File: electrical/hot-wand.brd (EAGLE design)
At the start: 112 x 72 mm, 186 parts, among them IC1 12V R-78K12-2.0, IC2 3V3 R-78K3.3, Q1 STP19NF20, Q2 IRF510, Q3 BC846B, Q4 SIRS5800DP-T1-GE3, Q5 2N7002K, Q6 DMTH64M2LPDWQ-13, Q7 G3404, U1 TPS54560DDA, U2 1EDN8511BXUSA1, U3 INA138, U4 LM74700QDBVTQ1, U5 AP53781, U6 SSD1306-4PIN-0.91N-VERT, U7 STM32F030F4P6, Y1 27.12 MHz 10pF

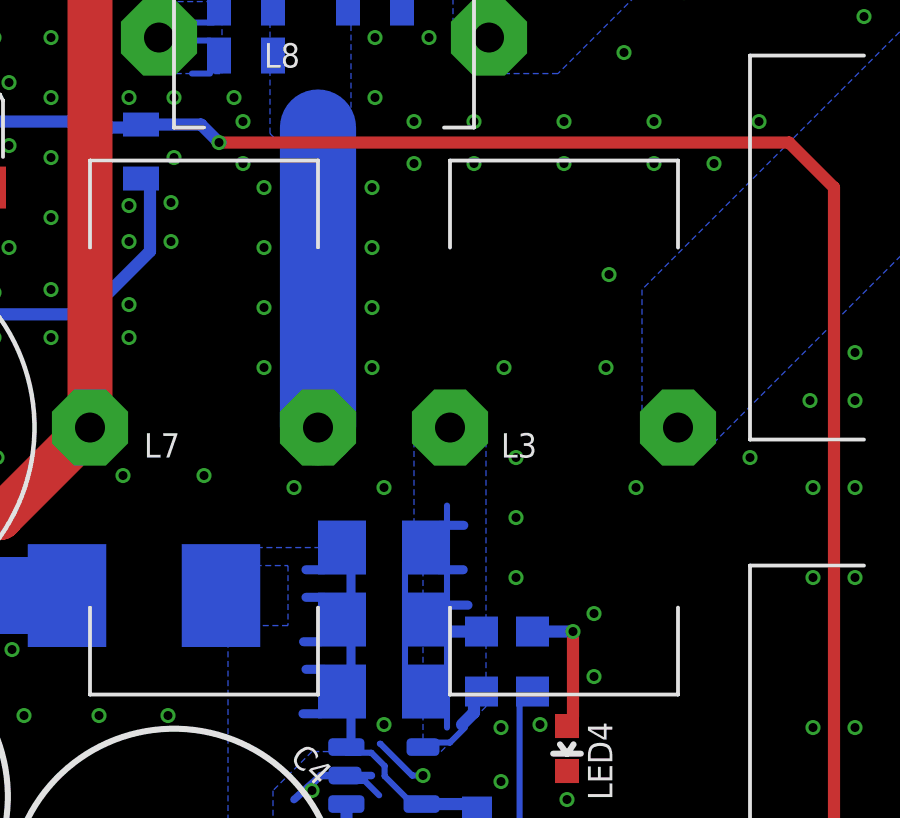
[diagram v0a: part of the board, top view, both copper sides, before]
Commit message: added another TVS diode to protect the buck converter
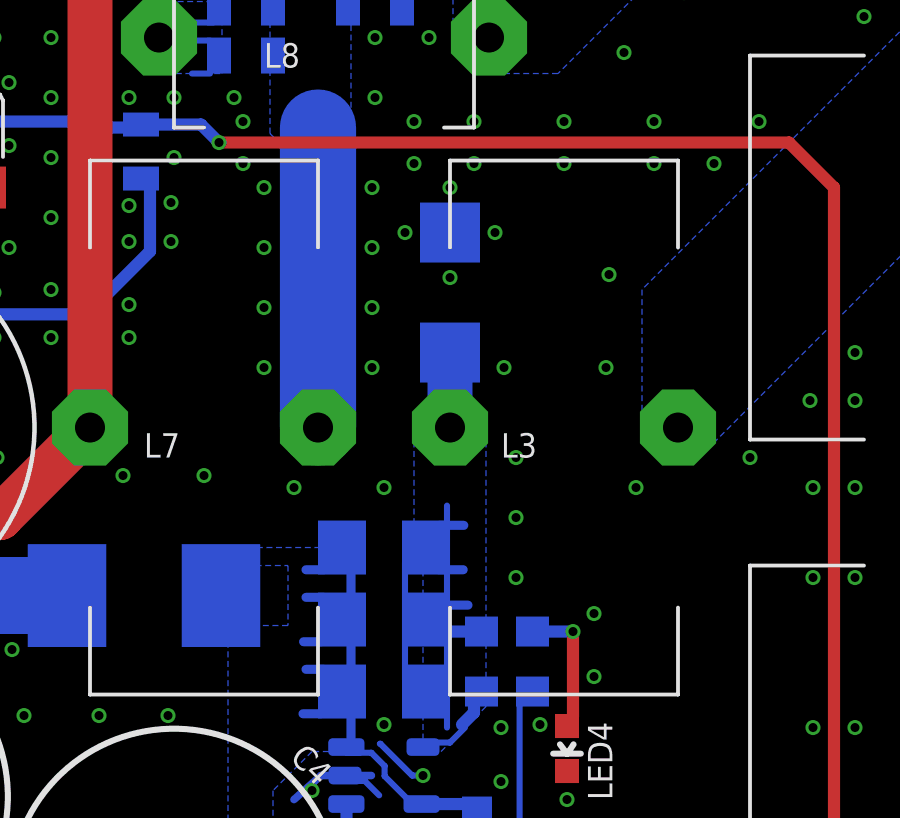
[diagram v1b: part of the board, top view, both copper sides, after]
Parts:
- added TVS6: SMAJ22A, hot-wand:SMA
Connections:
- net +24V: now also TVS6.C
- net GND: now also TVS6.A
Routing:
- net +24V: track 18.5 -> 21.0 mm
- net GND: vias 651 -> 655
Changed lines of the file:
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@@
 </polygon>
 <polygon width="0.01" layer="254">
-<vertex x="62.7" y="58"/>
+<vertex x="67.4" y="58"/>
 <vertex x="69.1" y="58"/>
 <vertex x="73.8" y="62.7"/>
 <vertex x="80.9" y="62.7"/>
 <vertex x="70.4" y="52.2"/>
-<vertex x="70.4" y="48.7"/>
-<vertex x="62.7" y="48.7"/>
+<vertex x="67.4" y="52.2"/>
 </polygon>
 <rectangle x1="35.8" y1="20.9" x2="37.4" y2="22.3" layer="32"/>
@@
 <attribute name="NAME" x="3.878" y="9.87" size="0.8128" layer="25" font="vector" rot="R270"/>
 <attribute name="VALUE" x="-1.102" y="21.67" size="1.27" layer="27" font="vector" rot="R270"/>
+</element>
+<element name="TVS6" library="hot-wand" package="SMA" value="SMAJ22A" x="65.2" y="51.5" smashed="yes" rot="MR90">
+<attribute name="NAME" x="67.5" y="49.25" size="0.8128" layer="26" ratio="10" rot="MR90"/>
+<attribute name="VALUE" x="68.5" y="49.25" size="0.8128" layer="28" ratio="10" rot="MR90"/>
+<attribute name="JLCPCBPART" value="C41376403" x="65.2" y="51.5" size="1.778" layer="28" rot="MR90" display="off"/>
 </element>
 </elements>
@@
 <via x="31.02" y="38" extent="1-16" drill="0.3" shape="octagon"/>
 <via x="28.92" y="35" extent="1-16" drill="0.3" shape="octagon"/>
+<contactref element="TVS6" pad="A"/>
+<via x="65.2" y="55" extent="1-16" drill="0.3" shape="octagon"/>
+<via x="66.7" y="53.5" extent="1-16" drill="0.3" shape="octagon"/>
+<via x="63.7" y="53.5" extent="1-16" drill="0.3" shape="octagon"/>
+<via x="65.2" y="52" extent="1-16" drill="0.3" shape="octagon"/>
 </signal>
 <signal name="RF-OUT">
@@
 <wire x1="63.7" y1="38.6" x2="63.7" y2="42.5" width="0.2032" layer="16"/>
 <wire x1="66.3" y1="40.2" x2="66.25" y2="40.2" width="0.4064" layer="16"/>
-<wire x1="66.2" y1="40.2" x2="64.9" y2="40.2" width="0.4064" layer="16"/>
+<wire x1="66.25" y1="40.2" x2="64.9" y2="40.2" width="0.4064" layer="16"/>
 <wire x1="63.7" y1="38.6" x2="64.1" y2="38.2" width="0.2032" layer="16"/>
 <wire x1="64.1" y1="38.2" x2="64.4" y2="38.2" width="0.2032" layer="16"/>
-<wire x1="66.25" y1="40.2" x2="66.2" y2="40.2" width="0.4064" layer="16"/>
 <wire x1="64.84" y1="43.74" x2="65.66" y2="43.74" width="0.3048" layer="16"/>
 <wire x1="64.82" y1="42.26" x2="65.64" y2="42.26" width="0.3048" layer="16"/>
 <wire x1="64.98" y1="41.08" x2="65.8" y2="41.08" width="0.3048" layer="16"/>
+<contactref element="TVS6" pad="C"/>
+<wire x1="65.2" y1="47" x2="65.2" y2="49.5" width="1.5" layer="16"/>
 </signal>
 <signal name="RF-GATE">

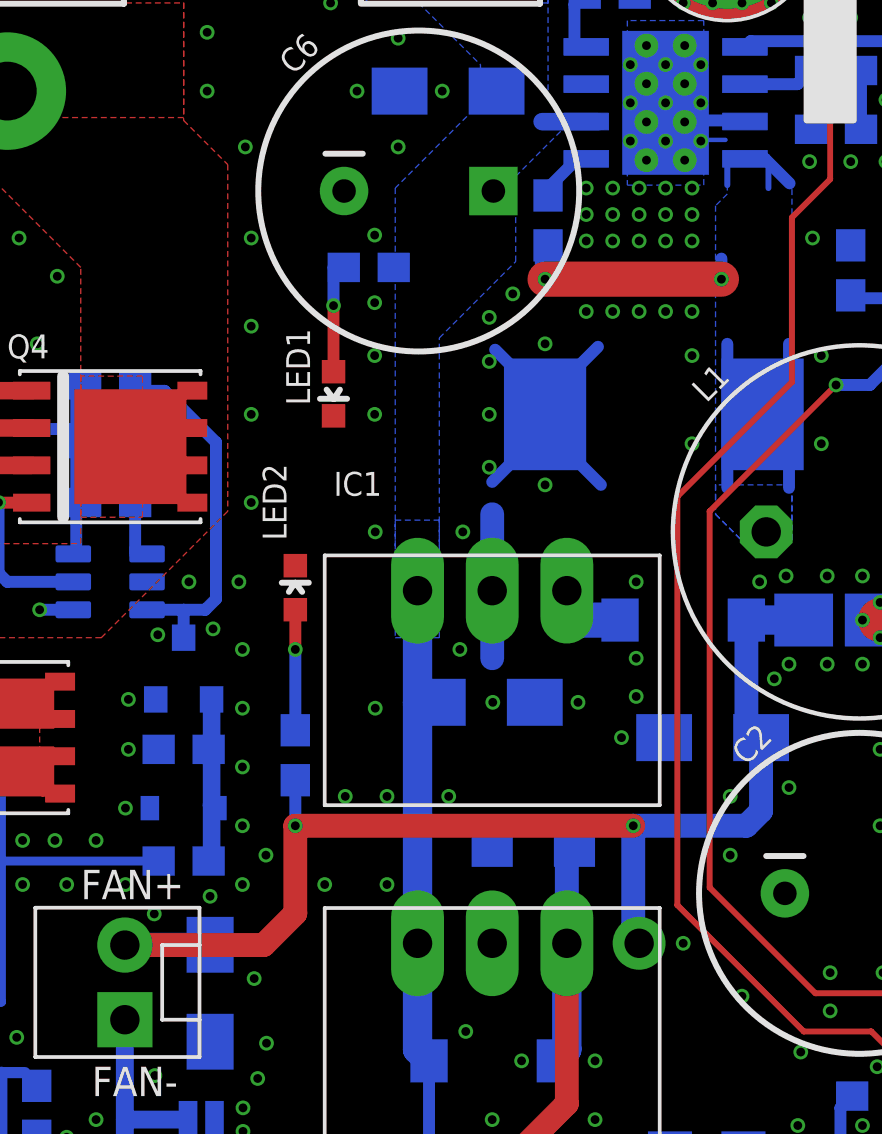
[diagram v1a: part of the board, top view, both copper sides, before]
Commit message: added out-to-in diode for buck converter
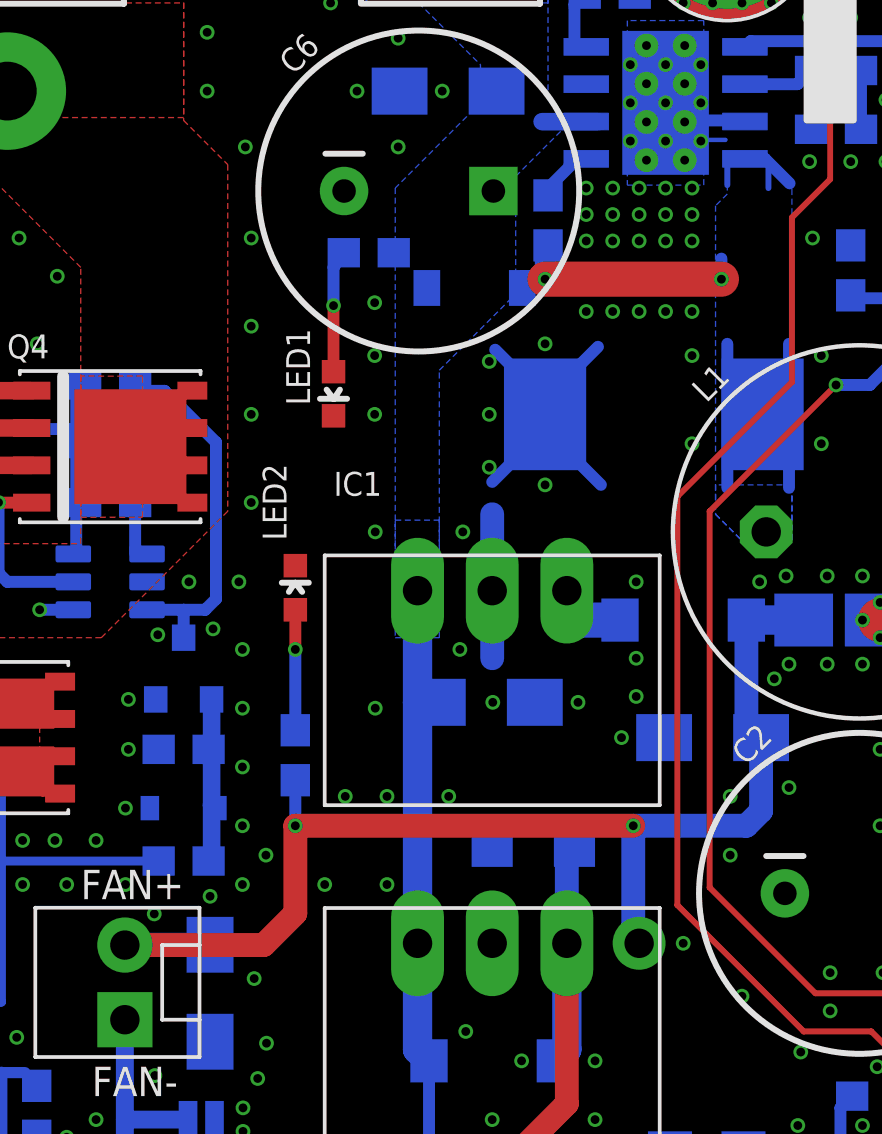
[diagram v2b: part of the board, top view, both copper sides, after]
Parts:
- added D13: 2A 60V, hot-wand:SOD123FL
- moved R38 0.50 mm to (28.3, 56.5)
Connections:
- net DC-IN: now also D13.C
- net N$23: now also D13.A
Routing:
- net N$23: track 21.9 -> 23.0 mm
- net GND: vias 655 -> 652
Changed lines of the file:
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@@
 </element>
 <element name="D1" library="hot-wand" package="SMC" value="STPS3L60S" x="38" y="51" smashed="yes" rot="MR0">
-<attribute name="NAME" x="33.659" y="53.559" size="0.8128" layer="26" font="vector" rot="MR0"/>
+<attribute name="NAME" x="31.941" y="51.459" size="0.8128" layer="26" font="vector" rot="MR270"/>
 <attribute name="JLCPARTNUM" value="C2971007" x="38" y="51" size="1.778" layer="28" rot="MR0" display="off"/>
 </element>
@@
 <attribute name="JLC-DNP" value="1" x="30.9" y="9.8" size="1.778" layer="27" display="off"/>
 </element>
-<element name="R38" library="hot-wand" package="0603-RES" value="2K2" x="28.3" y="56" smashed="yes" rot="MR0">
-<attribute name="NAME" x="26.589" y="55.662" size="0.8128" layer="26" font="vector" rot="MR0"/>
-<attribute name="VALUE" x="26.616" y="54.557" size="0.8128" layer="28" font="vector" rot="MR0"/>
-<attribute name="JLCPARTNUM" value="C4190" x="28.3" y="56" size="1.778" layer="28" rot="MR0" display="off"/>
+<element name="R38" library="hot-wand" package="0603-RES" value="2K2" x="28.3" y="56.5" smashed="yes" rot="MR0">
+<attribute name="NAME" x="26.589" y="56.162" size="0.8128" layer="26" font="vector" rot="MR0"/>
+<attribute name="VALUE" x="26.616" y="55.057" size="0.8128" layer="28" font="vector" rot="MR0"/>
+<attribute name="JLCPARTNUM" value="C4190" x="28.3" y="56.5" size="1.778" layer="28" rot="MR0" display="off"/>
 </element>
 <element name="R39" library="hot-wand" package="0603-RES" value="2K2" x="25.8" y="39.4" smashed="yes" rot="MR90">
@@
 <attribute name="VALUE" x="68.5" y="49.25" size="0.8128" layer="28" ratio="10" rot="MR90"/>
 <attribute name="JLCPCBPART" value="C41376403" x="65.2" y="51.5" size="1.778" layer="28" rot="MR90" display="off"/>
+</element>
+<element name="D13" library="hot-wand" package="SOD123FL" value="2A 60V" x="31.9" y="55.3" smashed="yes" rot="MR180">
+<attribute name="JLCPARTNUM" value="C53340922" x="31.9" y="55.3" size="1.778" layer="28" rot="MR180" display="off"/>
+<attribute name="PARTNUM" value="STPS2L60ZFY" x="31.9" y="55.3" size="1.778" layer="28" rot="MR180" display="off"/>
+<attribute name="NAME" x="33.3" y="56.3" size="0.8128" layer="26" rot="MR0"/>
 </element>
 </elements>
@@
 <via x="84" y="10" extent="1-16" drill="0.3" shape="octagon"/>
 <via x="32.4" y="52.8" extent="1-16" drill="0.3" shape="octagon"/>
-<via x="28.5" y="57.1" extent="1-16" drill="0.3" shape="octagon"/>
 <via x="28.5" y="54.8" extent="1-16" drill="0.3" shape="octagon"/>
 <via x="28.5" y="53" extent="1-16" drill="0.3" shape="octagon"/>
@@
 <via x="38.4" y="54.5" extent="1-16" drill="0.3" shape="octagon"/>
 <via x="39.3" y="54.5" extent="1-16" drill="0.3" shape="octagon"/>
-<via x="33.2" y="55.1" extent="1-16" drill="0.3" shape="octagon"/>
-<via x="32.4" y="54.3" extent="1-16" drill="0.3" shape="octagon"/>
 <via x="77" y="62.6" extent="1-16" drill="0.3" shape="octagon"/>
 <via x="75" y="62.6" extent="1-16" drill="0.3" shape="octagon"/>
@@
 <vertex x="29.2" y="43.4"/>
 <vertex x="30.7" y="43.4"/>
-<vertex x="30.7" y="53.6"/>
-<vertex x="33.3" y="56.2"/>
+<vertex x="30.7" y="52.5"/>
+<vertex x="33.3" y="55.1"/>
 <vertex x="33.3" y="59.1"/>
 <vertex x="34.9" y="60.7"/>
@@
 <wire x1="30.4" y1="25.85" x2="30.35" y2="25.9" width="0.4064" layer="16"/>
 <wire x1="30.35" y1="25.9" x2="30.35" y2="29" width="0.4064" layer="16"/>
-<wire x1="29.96" y1="33" x2="29.96" y2="41.1" width="1" layer="16"/>
+<wire x1="29.96" y1="33" x2="29.96" y2="41.2" width="1" layer="16"/>
 <wire x1="29.96" y1="41.2" x2="29.96" y2="45" width="1" layer="16"/>
 <wire x1="30.65" y1="41.2" x2="29.96" y2="41.2" width="1" layer="16"/>
-<wire x1="29.96" y1="41.2" x2="29.96" y2="41.1" width="1" layer="16"/>
+<contactref element="D13" pad="C"/>
 </signal>
 <signal name="N$19">
@@
 <via x="40.3" y="55.6" extent="1-16" drill="0.3" shape="octagon"/>
 <wire x1="40.3" y1="55.6" x2="40.3" y2="56.3" width="0.4064" layer="16"/>
+<contactref element="D13" pad="A"/>
+<wire x1="34.3" y1="55.6" x2="33.525" y2="55.6" width="0.6096" layer="16"/>
+<wire x1="33.525" y1="55.6" x2="33.525" y2="55.3" width="0.6096" layer="16"/>
 </signal>
 <signal name="N$24">
@@
 <via x="27.1" y="54.7" extent="1-16" drill="0.3" shape="octagon"/>
 <wire x1="27.1" y1="54.7" x2="27.1" y2="56" width="0.4064" layer="16"/>
-<wire x1="27.1" y1="56" x2="27.45" y2="56" width="0.4064" layer="16"/>
+<wire x1="27.1" y1="56" x2="27.45" y2="56.5" width="0.4064" layer="16"/>
 </signal>
 <signal name="N$47">

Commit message: Update hot-wand.brd
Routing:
- net GND: track 143.3 -> 146.4 mm
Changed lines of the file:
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@@
 <via x="63.7" y="53.5" extent="1-16" drill="0.3" shape="octagon"/>
 <via x="65.2" y="52" extent="1-16" drill="0.3" shape="octagon"/>
+<wire x1="64.2" y1="14.5" x2="65.8" y2="14.5" width="0.6096" layer="16"/>
+<wire x1="65.8" y1="14.5" x2="66.9" y2="13.4" width="0.6096" layer="16"/>
 </signal>
 <signal name="RF-OUT">

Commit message: changed a resistor that set the buck converter output voltage
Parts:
- R4: value 6K8 -> 22K
- TVS6: value SMAJ22A -> SMAJ24CA
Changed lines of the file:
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@@
 <attribute name="JLCPARTNUM" value="C4190" x="103.9" y="8.9" size="1.778" layer="28" rot="MR270" display="off"/>
 </element>
-<element name="R4" library="hot-wand" package="0603-RES" value="6K8" x="48.8" y="51.6" smashed="yes" rot="MR270">
+<element name="R4" library="hot-wand" package="0603-RES" value="22K" x="48.8" y="51.6" smashed="yes" rot="MR270">
 <attribute name="NAME" x="49.238" y="50.089" size="0.8128" layer="26" font="vector" rot="MR270"/>
 <attribute name="VALUE" x="48.043" y="50.416" size="0.8128" layer="28" font="vector" rot="MR270"/>
-<attribute name="JLCPARTNUM" value="C23212" x="48.8" y="51.6" size="1.778" layer="28" rot="MR270" display="off"/>
+<attribute name="JLCPARTNUM" value="C31850" x="48.8" y="51.6" size="1.778" layer="28" rot="MR270" display="off"/>
 </element>
 <element name="VR1" library="hot-wand" package="TRIM_35WR1KLFTR_V2" value="10K" x="48.8" y="56.7" smashed="yes" rot="R90">
@@
 <attribute name="VALUE" x="-1.102" y="21.67" size="1.27" layer="27" font="vector" rot="R270"/>
 </element>
-<element name="TVS6" library="hot-wand" package="SMA" value="SMAJ22A" x="65.2" y="51.5" smashed="yes" rot="MR90">
+<element name="TVS6" library="hot-wand" package="SMA" value="SMAJ24CA" x="65.2" y="51.5" smashed="yes" rot="MR90">
 <attribute name="NAME" x="67.5" y="49.25" size="0.8128" layer="26" ratio="10" rot="MR90"/>
 <attribute name="VALUE" x="68.5" y="49.25" size="0.8128" layer="28" ratio="10" rot="MR90"/>
-<attribute name="JLCPCBPART" value="C41376403" x="65.2" y="51.5" size="1.778" layer="28" rot="MR90" display="off"/>
+<attribute name="JLCPCBPART" value="C148223" x="65.2" y="51.5" size="1.778" layer="28" rot="MR90" display="off"/>
 </element>
 <element name="D13" library="hot-wand" package="SOD123FL" value="2A 60V" x="31.9" y="55.3" smashed="yes" rot="MR180">

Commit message: changed that 22V zener to 24V
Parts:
- D2: value BZT52C22 -> BZT52C24
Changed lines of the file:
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@@
 <attribute name="JLCPARTNUM" value="C845027" x="55" y="41.4" size="1.778" layer="28" rot="MR180" display="off"/>
 </element>
-<element name="D2" library="hot-wand" package="SOD123FL" value="BZT52C22" x="53.1" y="52.4" smashed="yes" rot="MR90">
+<element name="D2" library="hot-wand" package="SOD123FL" value="BZT52C24" x="53.1" y="52.4" smashed="yes" rot="MR90">
 <attribute name="NAME" x="53.5" y="50.1" size="0.8128" layer="26" font="vector" rot="MR270"/>
-<attribute name="JLCPARTNUM" value="C173423" x="53.1" y="52.4" size="1.778" layer="28" rot="MR90" display="off"/>
+<attribute name="JLCPARTNUM" value="C2109" x="53.1" y="52.4" size="1.778" layer="28" rot="MR90" display="off"/>
 </element>
 <element name="JP3" library="hot-wand" package="XT30PW" value="XT-CONNECTOR-XT30PW" x="2" y="53" smashed="yes" rot="R90">

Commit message: current transformer footprint
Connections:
- net N$12: now also T1.P1; no longer T1.P2
- net N$2: now also T1.S1B, T1.S2A; no longer T1.3, T1.4
- net N$5: now also T1.S2B; no longer T1.2
- net N$6: now also T1.S1A; no longer T1.1
- net RF-OUT: now also T1.P2; no longer T1.P1
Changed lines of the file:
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@@
 </element>
 <element name="D6" library="hot-wand" package="SOD123FL" value="4148" x="98.5" y="9" smashed="yes" rot="MR270">
-<attribute name="NAME" x="95.2" y="9.3" size="0.8128" layer="26" font="vector" rot="MR270"/>
+<attribute name="NAME" x="95.2" y="9.1" size="0.8128" layer="26" font="vector" rot="MR270"/>
 <attribute name="JLCPARTNUM" value="C917030" x="98.5" y="9" size="1.778" layer="28" rot="MR270" display="off"/>
 </element>
@@
 </signal>
 <signal name="RF-OUT">
-<contactref element="T1" pad="P1"/>
+<contactref element="T1" pad="P2"/>
 <contactref element="C33" pad="1"/>
 <contactref element="R21" pad="1"/>
@@
 </signal>
 <signal name="N$2">
-<contactref element="T1" pad="4"/>
-<contactref element="T1" pad="3"/>
+<contactref element="T1" pad="S1B"/>
+<contactref element="T1" pad="S2A"/>
 <contactref element="C33" pad="2"/>
 <wire x1="91.5" y1="10.1" x2="91.5" y2="6.1" width="0.6" layer="16"/>
@@
 <contactref element="D8" pad="A"/>
 <contactref element="D6" pad="C"/>
-<contactref element="T1" pad="2"/>
+<contactref element="T1" pad="S2B"/>
 <wire x1="95.975" y1="10.4" x2="96.2" y2="10.625" width="0.4064" layer="16"/>
 <wire x1="96.2" y1="10.625" x2="98.5" y2="10.625" width="0.4064" layer="16"/>
@@
 <contactref element="D7" pad="C"/>
 <contactref element="D5" pad="A"/>
-<contactref element="T1" pad="1"/>
+<contactref element="T1" pad="S1A"/>
 <wire x1="95.975" y1="1.8" x2="96.2" y2="1.575" width="0.4064" layer="16"/>
 <wire x1="96.2" y1="1.575" x2="98.5" y2="1.575" width="0.4064" layer="16"/>
@@
 <signal name="N$12">
 <contactref element="L6" pad="2"/>
-<contactref element="T1" pad="P2"/>
+<contactref element="T1" pad="P1"/>
 <contactref element="C27" pad="1"/>
 <contactref element="C28" pad="1"/>
